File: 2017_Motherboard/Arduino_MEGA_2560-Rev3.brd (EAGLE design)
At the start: 100 x 80 mm, 86 parts, among them IC1 NCP1117ST50T3G, IC2 FT232RL, IC3 ATMEGA2560-16AU, IC7 LMV358IDGKR, X1 POWERSUPPLY_DC21MMX, Y1 CSTCE16M0V53-R0 16MHZ

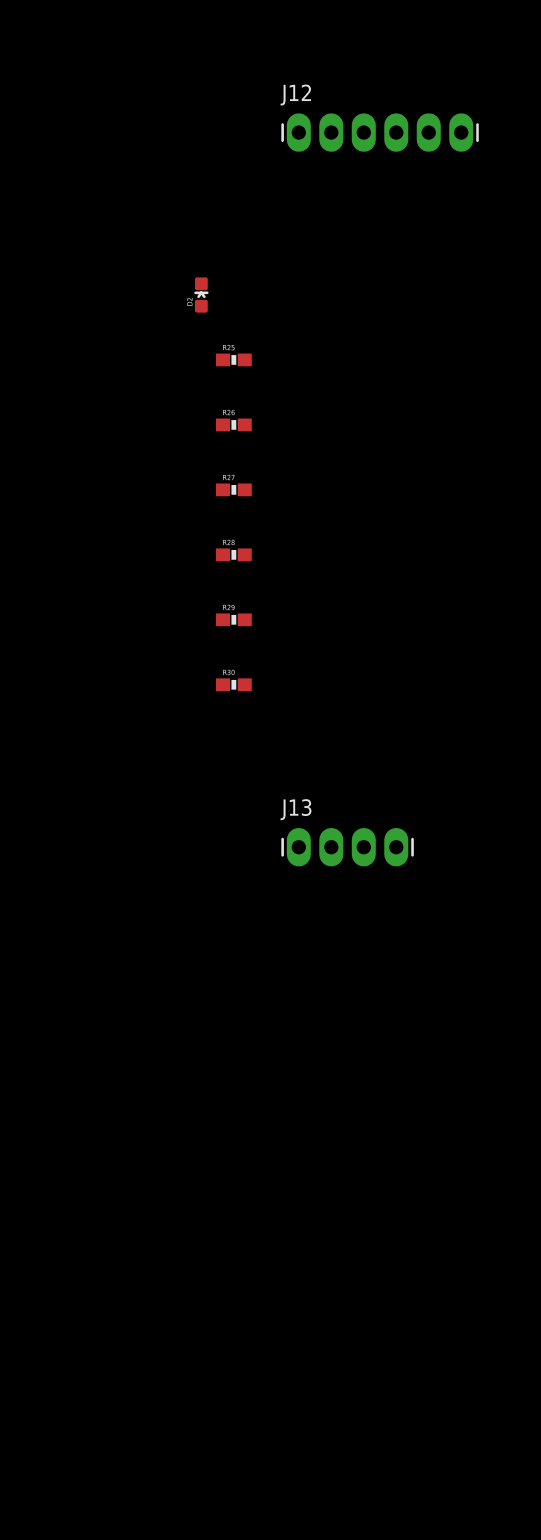
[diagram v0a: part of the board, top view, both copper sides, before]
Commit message: Added RS485 and video switching
Added several new parts to schematic. Hopefully the library transfers
with it. If not, download the maxim parts library for eagle
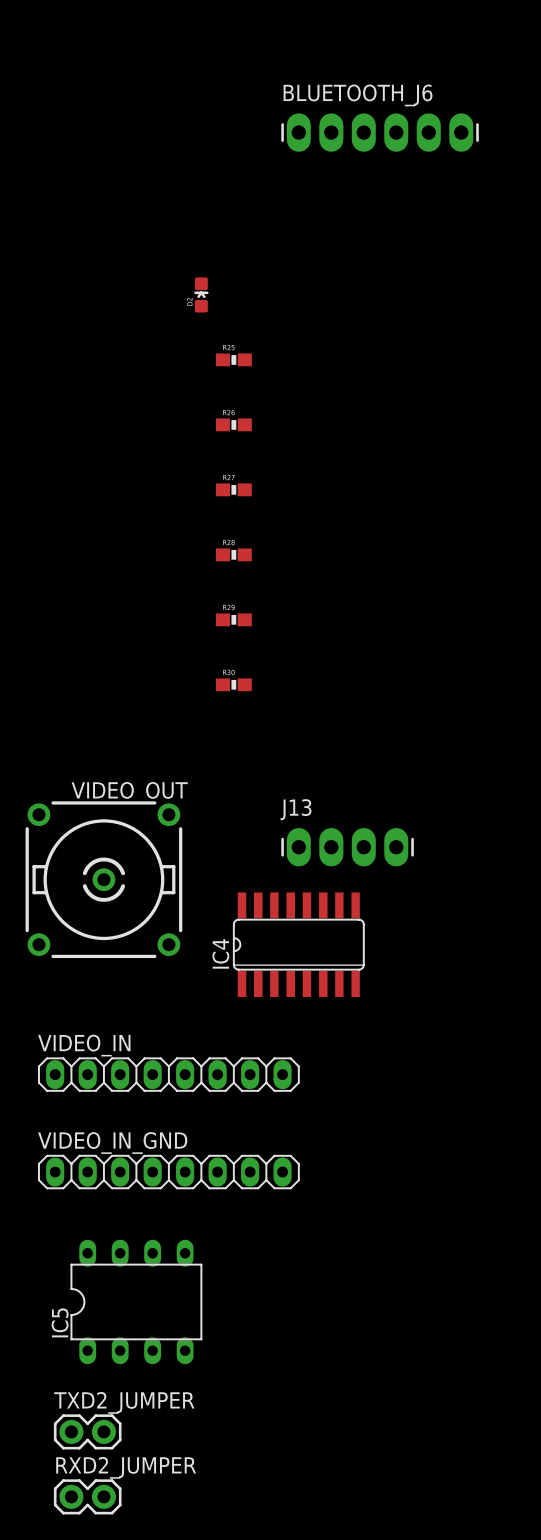
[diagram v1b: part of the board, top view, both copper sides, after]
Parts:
- added IC4: MAX4312ESE, maxim:SO16
- added IC5: MAX3468CPA, maxim:DIL08
- added RXD2_JUMPER, TXD2_JUMPER: (no value), SparkFun-Connectors:1X02
- added VIDEO_IN, VIDEO_IN_GND: 8x1F-H8.5, SmartPrj:1X08
- added VIDEO_OUT: A1944-50, con-coax:A1944
- renumbered J12 to BLUETOOTH_J6
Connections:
- new net RXD2_OUT: IC5.6, J13.2, RXD2_JUMPER.2
- new net TXD2_OUT: IC5.7, J13.1, TXD2_JUMPER.2
- new net VIDEO_OUT: IC4.16, VIDEO_OUT.1
- new net VID_0: IC4.5, VIDEO_IN.1
- new net VID_1: IC4.6, VIDEO_IN.2
- new net VID_2: IC4.7, VIDEO_IN.3
- new net VID_3: IC4.8, VIDEO_IN.4
- new net VID_4: IC4.9, VIDEO_IN.5
- new net VID_5: IC4.10, VIDEO_IN.6
- new net VID_6: IC4.11, VIDEO_IN.7
- new net VID_7: IC4.12, VIDEO_IN.8
- net +5V: now also IC4.4, IC5.8
- net GND: now also IC4.13, IC4.14, IC4.15, IC5.5, VIDEO_IN_GND.1, VIDEO_IN_GND.2, VIDEO_IN_GND.3, VIDEO_IN_GND.4, VIDEO_IN_GND.5, VIDEO_IN_GND.6, VIDEO_IN_GND.7, VIDEO_IN_GND.8, VIDEO_OUT.2, VIDEO_OUT.3, VIDEO_OUT.4, VIDEO_OUT.5
- net PA3: now also IC4.3
- net PA4: now also IC4.2
- net PA5: now also IC4.1
- net PA6: now also IC5.2
- net PA7: now also IC5.3
- net RXD2: now also IC5.1, RXD2_JUMPER.1; no longer J13.2
- net TXD2: now also IC5.4, TXD2_JUMPER.1; no longer J13.1

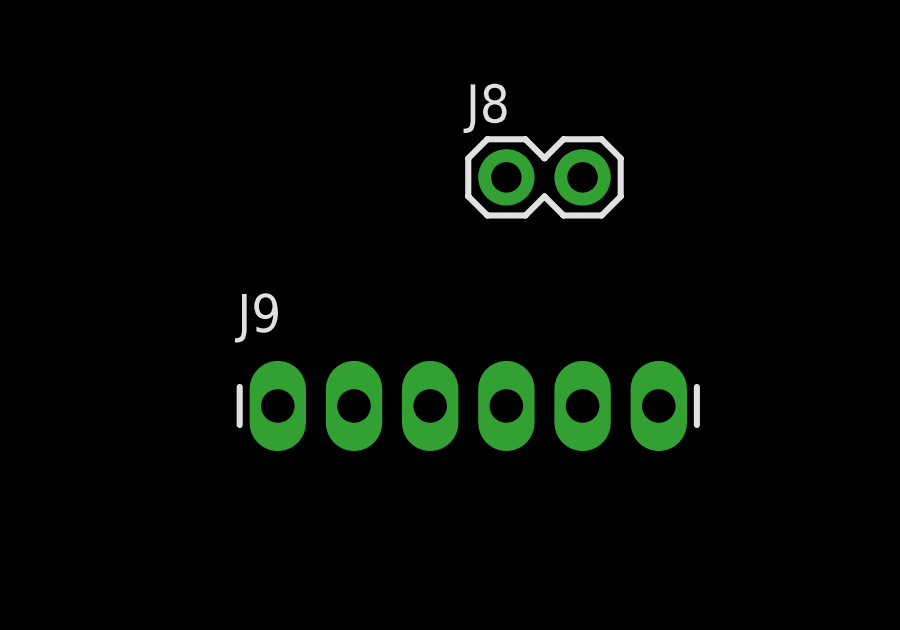
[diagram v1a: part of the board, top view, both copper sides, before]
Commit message: Updated part names
minor changes
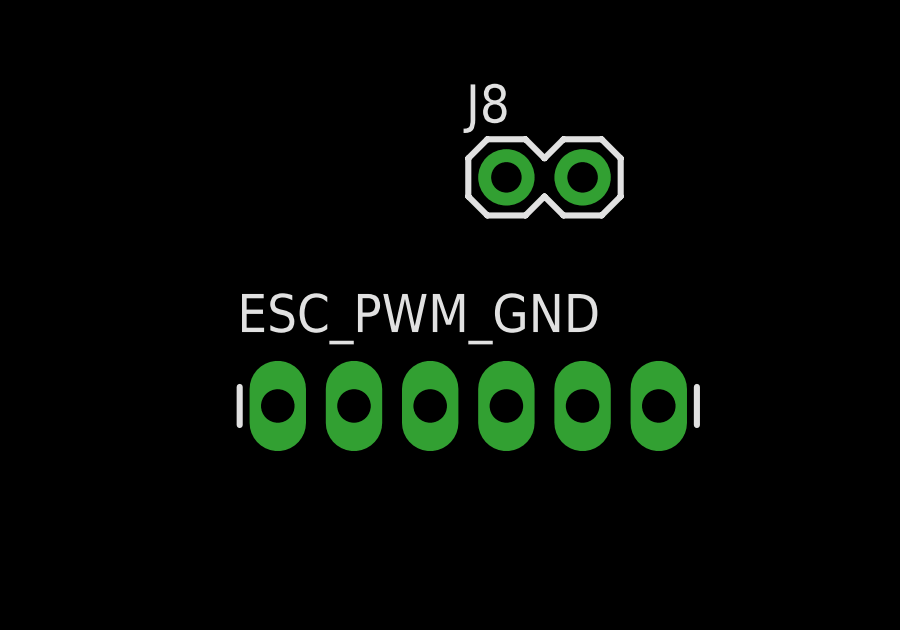
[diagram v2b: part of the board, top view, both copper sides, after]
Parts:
- renumbered J9 to ESC_PWM_GND
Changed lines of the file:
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@@
 <element name="J7" library="SparkFun-Connectors" package="1X02" value="" x="-7.62" y="-266.7"/>
 <element name="J8" library="SparkFun-Connectors" package="1X02" value="" x="-7.62" y="-287.02"/>
-<element name="J9" library="SparkFun-Connectors" package="1X06_LONGPADS" value="" x="-15.24" y="-294.64"/>
+<element name="ESC_PWM_GND" library="SparkFun-Connectors" package="1X06_LONGPADS" value="" x="-15.24" y="-294.64"/>
 <element name="J10" library="SparkFun-Connectors" package="1X02" value="" x="-15.24" y="-314.96"/>
 <element name="J11" library="SparkFun-Connectors" package="1X02" value="" x="-15.24" y="-335.28"/>
@@
 <contactref element="J2" pad="4"/>
 <contactref element="J2" pad="3"/>
-<contactref element="J9" pad="6"/>
-<contactref element="J9" pad="5"/>
-<contactref element="J9" pad="4"/>
-<contactref element="J9" pad="3"/>
-<contactref element="J9" pad="2"/>
-<contactref element="J9" pad="1"/>
+<contactref element="ESC_PWM_GND" pad="6"/>
+<contactref element="ESC_PWM_GND" pad="5"/>
+<contactref element="ESC_PWM_GND" pad="4"/>
+<contactref element="ESC_PWM_GND" pad="3"/>
+<contactref element="ESC_PWM_GND" pad="2"/>
+<contactref element="ESC_PWM_GND" pad="1"/>
 <contactref element="BLUETOOTH_J6" pad="3"/>
 <contactref element="R30" pad="1"/>

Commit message: Finalized schematic and began layout
FTDI chip is complete, although the AGND on it is a floating pin at the
moment. The RESET_B was changed to RESET on the schematic
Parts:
- moved R30 436.7 mm to (2.29, 37.3), turned to 180 degrees
- moved D2 408.4 mm to (2.29, 39.4), turned to 90 degrees
- moved J11 375.8 mm to (10.2, 39.6), turned to 90 degrees
- moved J10 368.8 mm to (3.05, 53.3)
- moved R19 281.5 mm to (24.9, 55.1), turned to 180 degrees
- moved R21 281.4 mm to (19.6, 57.1), turned to 180 degrees
- moved R24 278.6 mm to (16.0, 43.2)
- moved R18 273.2 mm to (24.9, 53.6), turned to 180 degrees
- moved R23 271.3 mm to (16.0, 41.7), turned to 180 degrees
- moved C17 270.9 mm to (15.2, 57.1)
- moved R22 270.3 mm to (16.0, 39.9)
- moved R20 269.3 mm to (16.0, 44.7)
- moved C18 265.8 mm to (11.9, 46.0), turned to 270 degrees
- moved C19 265.0 mm to (10.4, 46.0), turned to 270 degrees
- moved IC2 252.1 mm to (17.8, 50.8), turned to 90 degrees
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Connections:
- removed net RESET_B: R22.1
- net RESET: now also R22.1
- net V_USB: now also R23.2
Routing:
- net V_USB: track 0.00 -> 47.3 mm, vias 0 -> 2
- net GND: track 0.00 -> 30.5 mm, vias 0 -> 7
- net FTDI_3.3V: track 0.00 -> 20.2 mm
- net N$4: track 0.00 -> 18.2 mm, vias 0 -> 2
- net USBDP: track 0.00 -> 16.5 mm, vias 0 -> 2
- net USBDN: track 0.00 -> 15.6 mm
- net FTDI_CBUS1: track 0.00 -> 11.6 mm
- net FTDI_CBUS0: track 0.00 -> 7.30 mm
- net USB_GND: track 0.00 -> 6.96 mm
- net FTDI_CBUS2: track 0.00 -> 2.94 mm
- net SLEEP: track 0.00 -> 2.69 mm
- net POWER_EN: track 0.00 -> 2.54 mm
- net N$15: track 0.00 -> 2.03 mm
- added copper zone on layer 1, net +3V3
- added copper zone on layer 1, net +5V
- added copper zone on layer 16, net GND
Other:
- board text added: "Aground on the FTDI is not connected to anything at the moment"

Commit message: Motherboard routing
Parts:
- removed COMMUNICATION: 8x1F-H8.5, SmartPrj:1X08
- removed XIO: 18x2F-H8.5, SmartPrj:2X18
- added IC6: MAX4312ESE, maxim:SO16
- added J9: (no value), SparkFun-Connectors:1X02
- added JP1: (no value), pinhead:2X05
- added JP2: (no value), pinhead:2X09
- added R31, R33: 0, SparkFun-Resistors:0603-RES
- added R32, R34: inf, SparkFun-Resistors:0603-RES
- added VIDEO_OUT1: A1944-50, con-coax:A1944
- moved VIDEO_OUT 497.6 mm to (85.6, 69.8), turned to 270 degrees
- moved VIDEO_IN_GND 495.9 mm to (96.8, 43.7), turned to 270 degrees
- moved RXD2_JUMPER 489.3 mm to (82.5, 13.2), turned to 90 degrees
- moved TXD2_JUMPER 487.7 mm to (96.8, 13.0), turned to 90 degrees
- moved VIDEO_IN 487.6 mm to (93.2, 43.7), turned to 90 degrees
- moved IC4 485.7 mm to (85.1, 56.1)
- moved IC5 476.2 mm to (89.4, 14.5)
- moved R28 455.8 mm to (59.4, 60.2), turned to 180 degrees
- moved J13 445.9 mm to (85.9, 22.9)
- moved R25 440.1 mm to (12.2, 65.5)
- moved R26 440.1 mm to (12.2, 60.5)
- moved R29 430.4 mm to (31.5, 33.5), turned to 270 degrees
- moved BLUETOOTH_J6 424.5 mm to (56.9, 62.7), turned to 90 degrees
- moved R27 392.4 mm to (10.9, 7.62), turned to 180 degrees
- moved J8 362.4 mm to (10.7, 74.9)
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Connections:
- new net FB: IC4.15, IC6.15
- new net N$17: R31.2, R32.1
- new net N$18: R33.2, R34.1
- new net VIDEO_OUT1: IC6.16, R33.1, VIDEO_OUT1.1
- net +5V: now also IC4.14, IC6.14, IC6.4, JP1.1, JP1.2; no longer XIO.1, XIO.2
- net GND: now also IC6.13, JP2.17, JP2.18, R32.2, R34.2, VIDEO_OUT1.2, VIDEO_OUT1.3, VIDEO_OUT1.4, VIDEO_OUT1.5; no longer IC4.14, IC4.15, XIO.35, XIO.36
- net PA0: no longer XIO.3
- net PA1: no longer XIO.4
- net PA2: no longer XIO.5
- net PA3: now also IC6.3; no longer XIO.6
- net PA4: now also IC6.2; no longer XIO.7
- net PA5: now also IC6.1; no longer XIO.8
- net PA6: no longer XIO.9
- net PA7: no longer XIO.10
- net PB0: now also JP2.16; no longer XIO.34
- net PB1: now also JP2.15; no longer XIO.33
- net PB2: now also JP2.14; no longer XIO.32
- net PB3: now also JP2.13; no longer XIO.31
- net PC0: now also JP1.10; no longer XIO.18
- net PC1: now also JP1.9; no longer XIO.17
- net PC2: now also JP1.8; no longer XIO.16
- net PC3: now also JP1.7; no longer XIO.15
- net PC4: now also JP1.6; no longer XIO.14
- net PC5: now also JP1.5; no longer XIO.13
- net PC6: now also JP1.4; no longer XIO.12
- net PC7: now also JP1.3; no longer XIO.11
- net PD7: now also JP2.1; no longer XIO.19
- net PG0: now also JP2.4; no longer XIO.22
- net PG1: now also JP2.3; no longer XIO.21
- net PG2: now also JP2.2; no longer XIO.20
- net PL0: now also JP2.12; no longer XIO.30
- net PL1: now also JP2.11; no longer XIO.29
- net PL2: now also JP2.10; no longer XIO.28
- net PL3: now also JP2.9; no longer XIO.27
- net PL4: now also JP2.8; no longer XIO.26
- net PL5: now also JP2.7; no longer XIO.25
- net PL6: now also JP2.6; no longer XIO.24
- net PL7: now also JP2.5; no longer XIO.23
- net RXD1: no longer COMMUNICATION.3
- net RXD2: no longer COMMUNICATION.5
- net RXD3: now also J9.1; no longer COMMUNICATION.7
- net SCL: no longer COMMUNICATION.1
- net SDA: no longer COMMUNICATION.2
- net TXD1: no longer COMMUNICATION.4
- net TXD2: no longer COMMUNICATION.6
- net TXD3: now also J9.2; no longer COMMUNICATION.8
- net VIDEO_OUT: now also R31.1
- net VID_0: now also IC6.5
- net VID_1: now also IC6.6
- net VID_2: now also IC6.7
- net VID_3: now also IC6.8
- net VID_4: now also IC6.9
- net VID_5: now also IC6.10
- net VID_6: now also IC6.11
- net VID_7: now also IC6.12
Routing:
- net GND: track 30.5 -> 46.8 mm, vias 7 -> 9
- net ADC1: track 0.00 -> 8.66 mm
- net ADC3: track 0.00 -> 7.72 mm
- net ADC0: track 0.00 -> 7.62 mm
- net ADC2: track 0.00 -> 7.36 mm
- net ADC7: track 0.00 -> 4.27 mm
- net ADC4: track 0.00 -> 3.84 mm
- net ADC5: track 0.00 -> 3.84 mm
- net ADC6: track 0.00 -> 3.74 mm
- net N$5: track 0.00 -> 2.66 mm
- net N$1: track 0.00 -> 2.66 mm
- net N$6: track 0.00 -> 2.65 mm
- net N$12: track 0.00 -> 2.65 mm
- net N$14: track 0.00 -> 2.65 mm
- net N$10: track 0.00 -> 2.65 mm
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- added copper zone on layer 1, net GND
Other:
- board size 100 x 80 mm -> 100 x 78 mm

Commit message: More motherboard tinkering
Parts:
- moved IC3 4.68 mm to (48.9, 39.4)

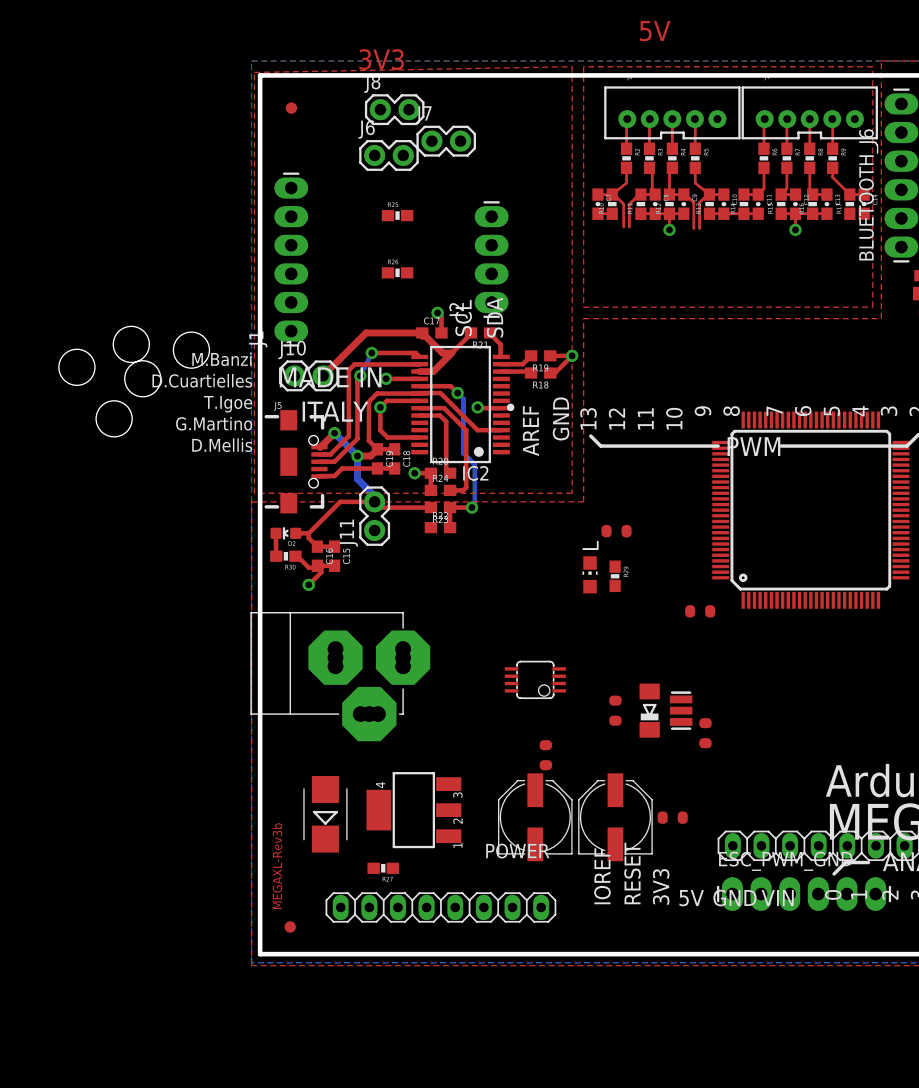
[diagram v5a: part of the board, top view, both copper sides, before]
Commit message: Routed power
Working on AREF plane
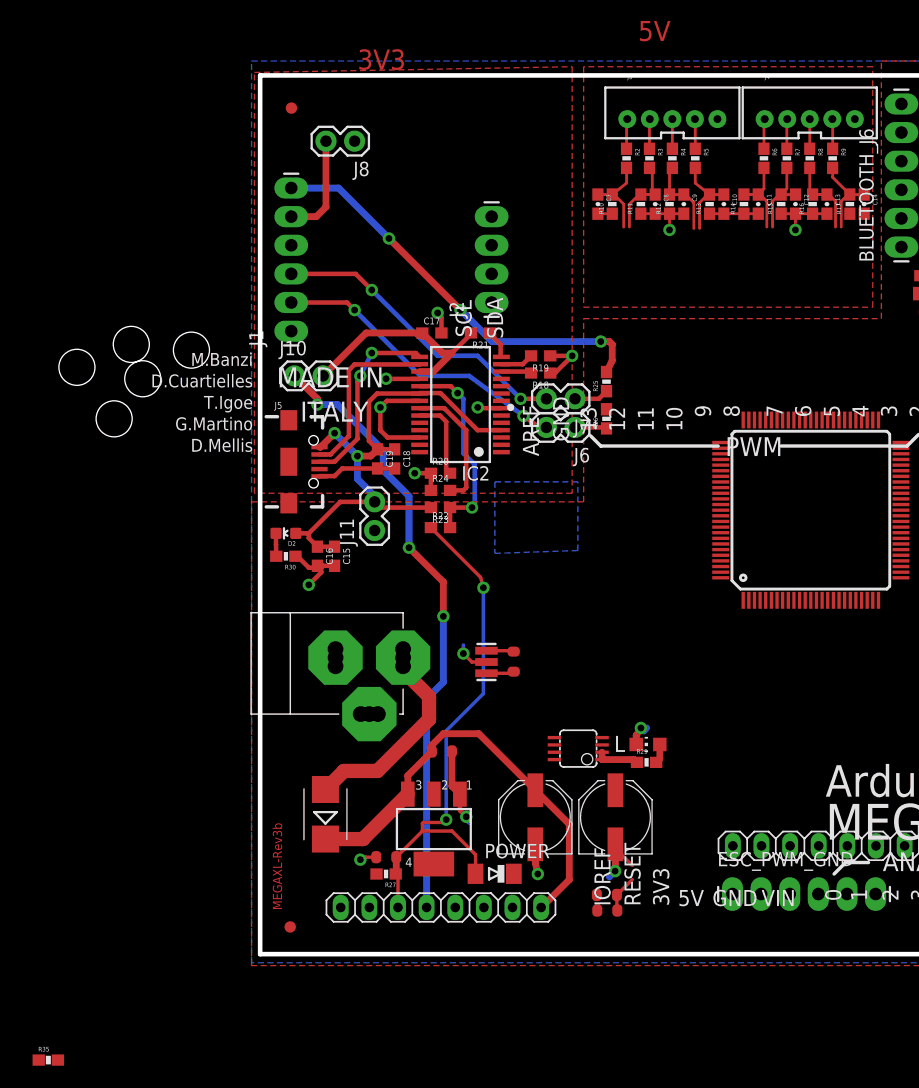
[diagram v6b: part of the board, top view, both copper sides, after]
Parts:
- removed C3: 100n, SmartPrj:C0603-ROUND
- added R35: (no value), SparkFun-Passives:0603-RES
- moved J6 30.0 mm to (27.9, 46.7), turned to 180 degrees
- moved C6 27.8 mm to (30.8, 3.87), turned to 0 degrees
- moved J7 26.2 mm to (27.9, 49.3), turned to 180 degrees
- moved C1 24.1 mm to (11.2, 8.60), turned to 180 degrees
- moved R25 23.7 mm to (30.7, 50.8), turned to 90 degrees
- moved R26 22.6 mm to (30.7, 47.5), turned to 90 degrees
- moved D3 20.0 mm to (20.8, 7.13), turned to 180 degrees
- moved R1 18.2 mm to (22.5, 26.0)
- moved Y1 17.8 mm to (20.1, 25.9)
- moved R29 16.7 mm to (34.3, 17.0), turned to 0 degrees
- moved L 15.9 mm to (34.4, 18.6), turned to 90 degrees
- moved C2 9.23 mm to (16.1, 18.0), turned to 0 degrees
- moved C4 9.01 mm to (30.8, 5.25)
- moved IC7 7.19 mm to (28.2, 18.2)
- moved J8 3.61 mm to (8.38, 72.1), turned to 180 degrees
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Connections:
- removed net AGND: IC2.25
- removed net INV: J1.6
- net +5V: now also J1.6
- net AREF: now also IC2.25, R35.2; no longer C3.1
- net GND: now also R35.1; no longer C3.2
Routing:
- net +3V3: track 0.00 -> 54.3 mm, vias 0 -> 3
- net RESET: track 0.00 -> 47.4 mm, vias 0 -> 2
- net VIN: track 0.00 -> 38.6 mm
- net +5V: track 0.00 -> 36.8 mm, vias 0 -> 3
- net N$9: track 0.00 -> 27.2 mm, vias 0 -> 2
- net N$11: track 0.00 -> 27.0 mm, vias 0 -> 2
- net GND: track 46.8 -> 72.6 mm, vias 9 -> 15
- net PWRIN: track 0.00 -> 18.2 mm
- net N$7: track 0.00 -> 9.28 mm
- net ADC6: track 3.74 -> 8.30 mm
- net ADC4: track 3.84 -> 8.41 mm
- net L13: track 0.00 -> 3.85 mm
- net ADC5: track 3.84 -> 7.14 mm
- net ADC7: track 4.27 -> 7.56 mm
- net SDA: track 0.00 -> 3.07 mm
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- added copper zone on layer 16, net AREF
